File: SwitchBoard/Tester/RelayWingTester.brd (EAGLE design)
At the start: 70.8 x 63.5 mm, 18 parts

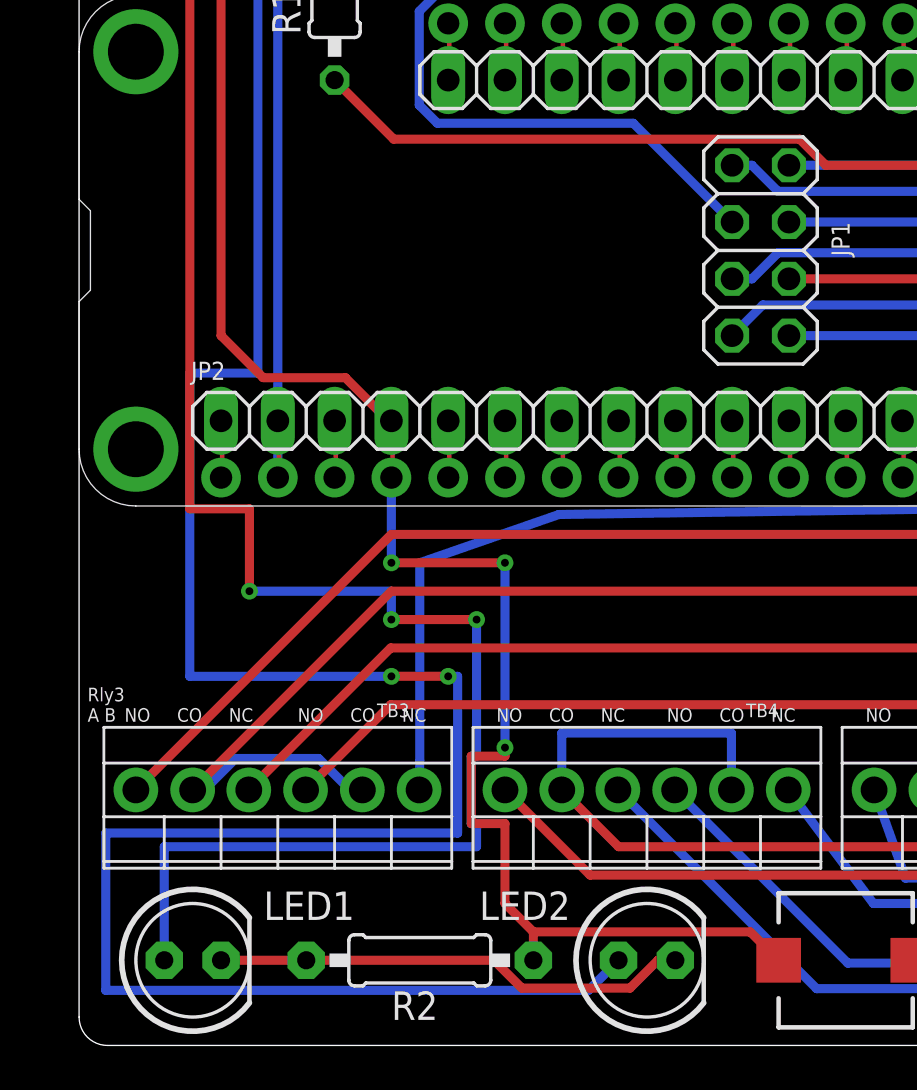
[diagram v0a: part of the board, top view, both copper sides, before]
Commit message: Added 2x2 header & silkscreen changes
This is a version that has no airwires and has a 2x2 header with the I2C bus and power and ground pulled out.   It does NOT have John's part number changes that took place after 5/28
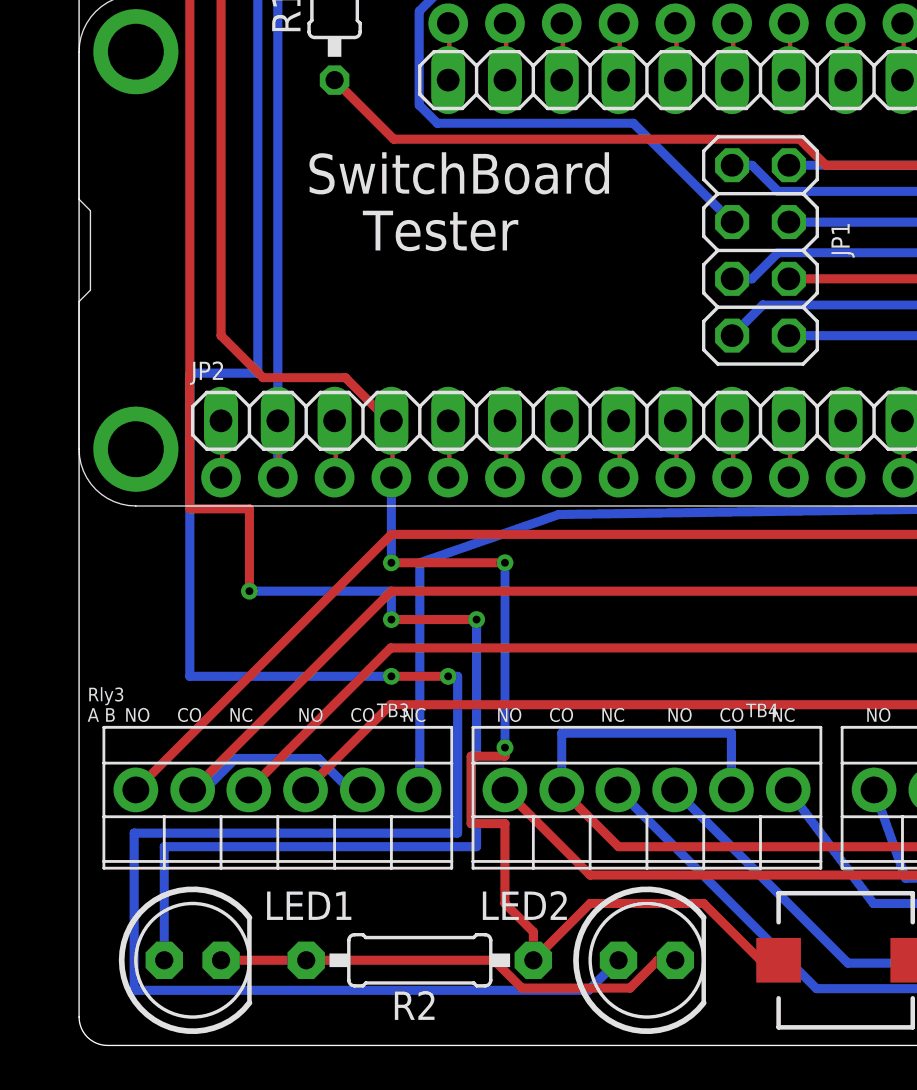
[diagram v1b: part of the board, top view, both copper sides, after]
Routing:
- net N$64: track 162.0 -> 159.4 mm
- net GND: track 134.4 -> 136.0 mm
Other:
- board text added: "SwitchBoard"
- board text added: "Tester"
